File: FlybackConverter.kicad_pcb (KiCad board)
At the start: 2 copper layers, 76.2 x 76.2 mm, 46 parts, among them J1 USB_C_Receptacle_PowerOnly_6P, T1 Transformer_1P_2S, U1 LNK6428K, U2 TPS25820DSST

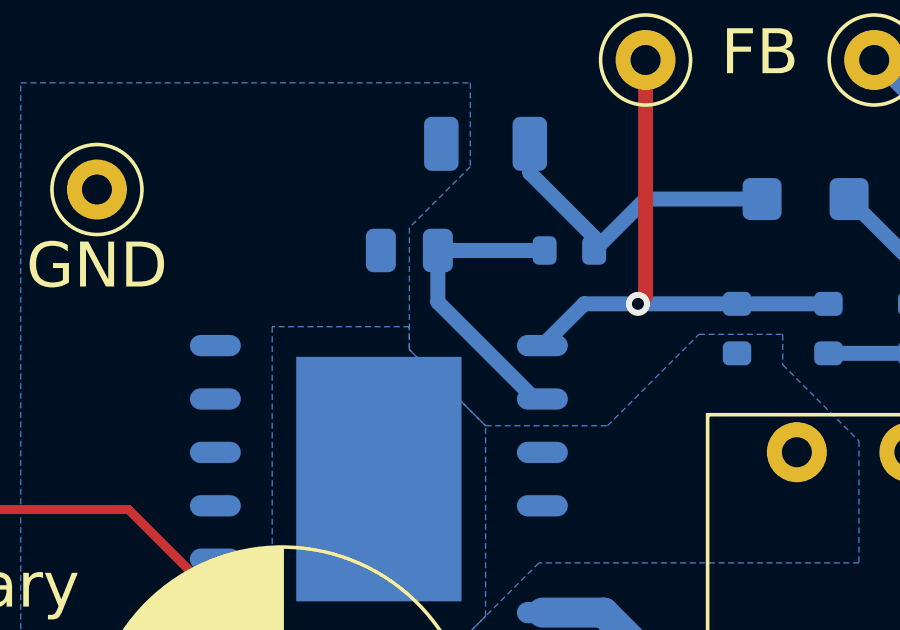
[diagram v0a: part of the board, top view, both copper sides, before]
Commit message: C7のフットプリントを1206に変更 #5
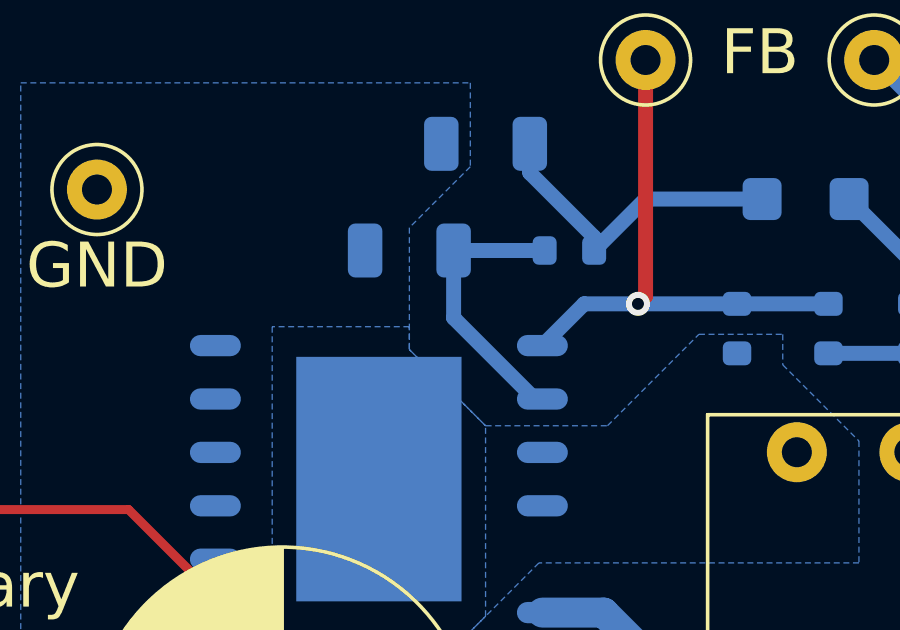
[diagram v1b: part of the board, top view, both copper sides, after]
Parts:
- C7: footprint Capacitor_SMD:C_0805_2012Metric -> Capacitor_SMD:C_1206_3216Metric
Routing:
- net Net-(U1-BP): track 10.1 -> 9.36 mm
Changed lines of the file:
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@@
     )
   )
-  (footprint "Capacitor_SMD:C_0805_2012Metric" (layer "B.Cu")
+  (footprint "Capacitor_SMD:C_1206_3216Metric" (layer "B.Cu")
     (at 147.066 62.23 180)
-    (descr "Capacitor SMD 0805 (2012 Metric), square (rectangular) end terminal, IPC_7351 nominal, (Body size source: IPC-SM-782 page 76, https://www.pcb-3d.com/wordpress/wp-content/uploads/ipc-sm-782a_amendment_1_and_2.pdf, https://docs.google.com/spreadsheets/d/1BsfQQcO9C6DZCsRaXUlFlo91Tg2WpOkGARC1WS5S8t0/edit?usp=sharing), generated with kicad-footprint-generator")
+    (descr "Capacitor SMD 1206 (3216 Metric), square (rectangular) end terminal, IPC_7351 nominal, (Body size source: IPC-SM-782 page 76, https://www.pcb-3d.com/wordpress/wp-content/uploads/ipc-sm-782a_amendment_1_and_2.pdf), generated with kicad-footprint-generator")
     (tags "capacitor")
     (property "Sheetfile" "FlybackConverter.kicad_sch")
@@
     (property "ki_keywords" "cap capacitor")
     (attr smd)
-    (fp_text reference "C7" (at 2.54 0) (layer "B.SilkS")
+    (fp_text reference "C7" (at 0 1.85) (layer "B.SilkS")
         (effects (font (size 1 1) (thickness 0.15)) (justify mirror))
     )
-    (fp_text value "1u" (at -2.985 -3.458) (layer "B.Fab")
+    (fp_text value "1u" (at 0 -1.85) (layer "B.Fab")
         (effects (font (size 1 1) (thickness 0.15)) (justify mirror))
     )
     (fp_text user "${REFERENCE}" (at 0 0) (layer "B.Fab")
-        (effects (font (size 0.5 0.5) (thickness 0.08)) (justify mirror))
+        (effects (font (size 0.8 0.8) (thickness 0.12)) (justify mirror))
     )
-    (fp_line (start -0.261252 -0.735) (end 0.261252 -0.735)
+    (fp_line (start -0.711252 -0.91) (end 0.711252 -0.91)
       (stroke (width 0.12) (type solid)) (layer "B.SilkS"))
-    (fp_line (start -0.261252 0.735) (end 0.261252 0.735)
+    (fp_line (start -0.711252 0.91) (end 0.711252 0.91)
       (stroke (width 0.12) (type solid)) (layer "B.SilkS"))
-    (fp_line (start -1.7 -0.98) (end -1.7 0.98)
+    (fp_line (start -2.3 -1.15) (end -2.3 1.15)
       (stroke (width 0.05) (type solid)) (layer "B.CrtYd"))
-    (fp_line (start -1.7 0.98) (end 1.7 0.98)
+    (fp_line (start -2.3 1.15) (end 2.3 1.15)
       (stroke (width 0.05) (type solid)) (layer "B.CrtYd"))
-    (fp_line (start 1.7 -0.98) (end -1.7 -0.98)
+    (fp_line (start 2.3 -1.15) (end -2.3 -1.15)
       (stroke (width 0.05) (type solid)) (layer "B.CrtYd"))
-    (fp_line (start 1.7 0.98) (end 1.7 -0.98)
+    (fp_line (start 2.3 1.15) (end 2.3 -1.15)
       (stroke (width 0.05) (type solid)) (layer "B.CrtYd"))
-    (fp_line (start -1 -0.625) (end -1 0.625)
+    (fp_line (start -1.6 -0.8) (end -1.6 0.8)
       (stroke (width 0.1) (type solid)) (layer "B.Fab"))
-    (fp_line (start -1 0.625) (end 1 0.625)
+    (fp_line (start -1.6 0.8) (end 1.6 0.8)
       (stroke (width 0.1) (type solid)) (layer "B.Fab"))
-    (fp_line (start 1 -0.625) (end -1 -0.625)
+    (fp_line (start 1.6 -0.8) (end -1.6 -0.8)
       (stroke (width 0.1) (type solid)) (layer "B.Fab"))
-    (fp_line (start 1 0.625) (end 1 -0.625)
+    (fp_line (start 1.6 0.8) (end 1.6 -0.8)
       (stroke (width 0.1) (type solid)) (layer "B.Fab"))
-    (pad "1" smd roundrect (at -0.95 0 180) (size 1 1.45) (layers "B.Cu" "B.Paste" "B.Mask") (roundrect_rratio 0.25)
+    (pad "1" smd roundrect (at -1.475 0 180) (size 1.15 1.8) (layers "B.Cu" "B.Paste" "B.Mask") (roundrect_rratio 0.217391)
       (net 9 "Net-(U1-BP)") (pintype "passive"))
-    (pad "2" smd roundrect (at 0.95 0 180) (size 1 1.45) (layers "B.Cu" "B.Paste" "B.Mask") (roundrect_rratio 0.25)
+    (pad "2" smd roundrect (at 1.475 0 180) (size 1.15 1.8) (layers "B.Cu" "B.Paste" "B.Mask") (roundrect_rratio 0.217391)
       (net 17 "Net-(T1-SB)") (pintype "passive"))
-    (model "${KICAD6_3DMODEL_DIR}/Capacitor_SMD.3dshapes/C_0805_2012Metric.wrl"
+    (model "${KICAD6_3DMODEL_DIR}/Capacitor_SMD.3dshapes/C_1206_3216Metric.wrl"
       (offset (xyz 0 0 0))
       (scale (xyz 1 1 1))
@@
   (segment (start 166.558 93.9755) (end 167.3245 94.742) (width 1) (layer "B.Cu") (net 8))
   (segment (start 166.558 91.186) (end 166.558 93.9755) (width 1) (layer "B.Cu") (net 8))
-  (segment (start 148.016 62.23) (end 151.575 62.23) (width 0.5) (layer "B.Cu") (net 9))
-  (segment (start 148.016 63.95) (end 151.246 67.18) (width 0.5) (layer "B.Cu") (net 9))
+  (segment (start 151.575 62.23) (end 148.541 62.23) (width 0.5) (layer "B.Cu") (net 9))
+  (segment (start 148.541 62.23) (end 148.541 64.475) (width 0.5) (layer "B.Cu") (net 9))
   (segment (start 151.246 67.18) (end 151.5 67.18) (width 0.5) (layer "B.Cu") (net 9))
-  (segment (start 148.016 62.23) (end 148.016 63.95) (width 0.5) (layer "B.Cu") (net 9))
+  (segment (start 148.541 64.475) (end 151.246 67.18) (width 0.5) (layer "B.Cu") (net 9))
   (segment (start 154.94 60.515) (end 158.824 60.515) (width 0.5) (layer "B.Cu") (net 10))
   (segment (start 153.225 62.23) (end 154.94 60.515) (width 0.5) (layer "B.Cu") (net 10))

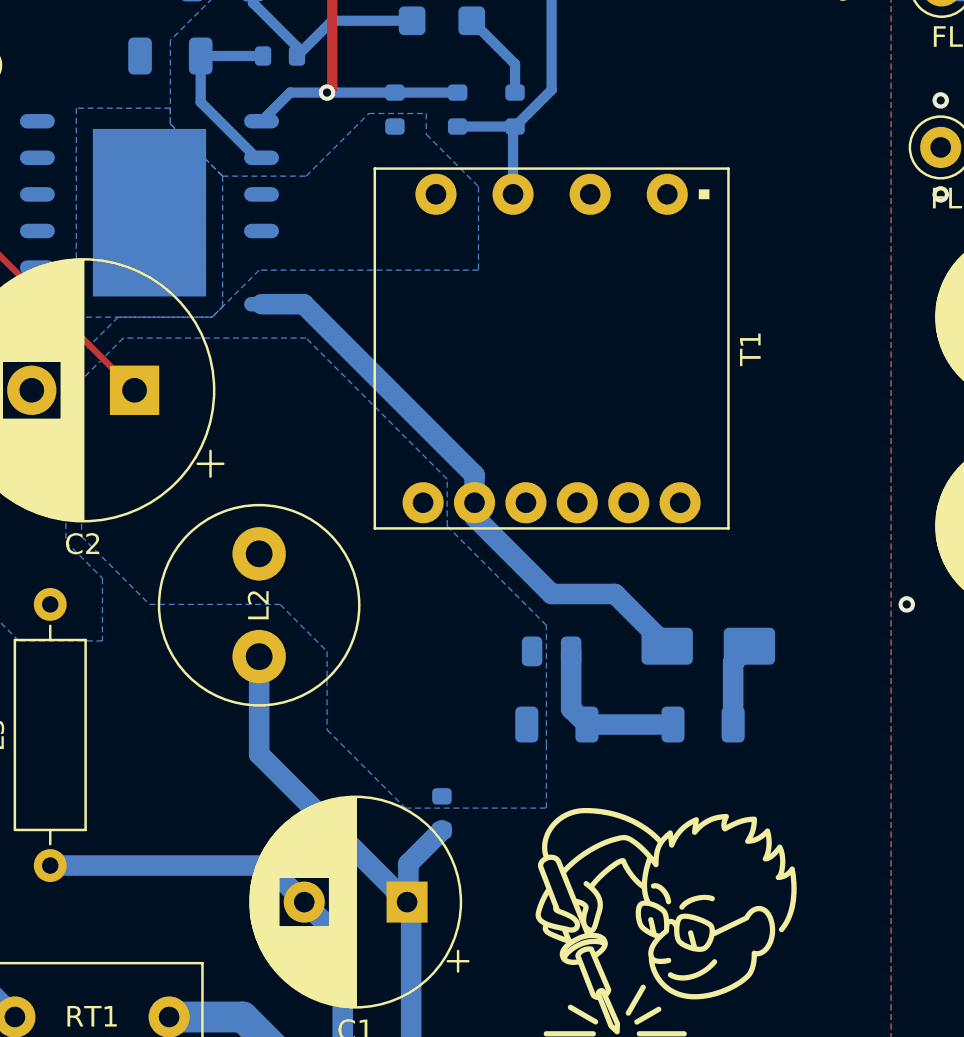
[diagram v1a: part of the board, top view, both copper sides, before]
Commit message: トランスのフットプリント修正、それに合わせて部品配置も調整 fix #6
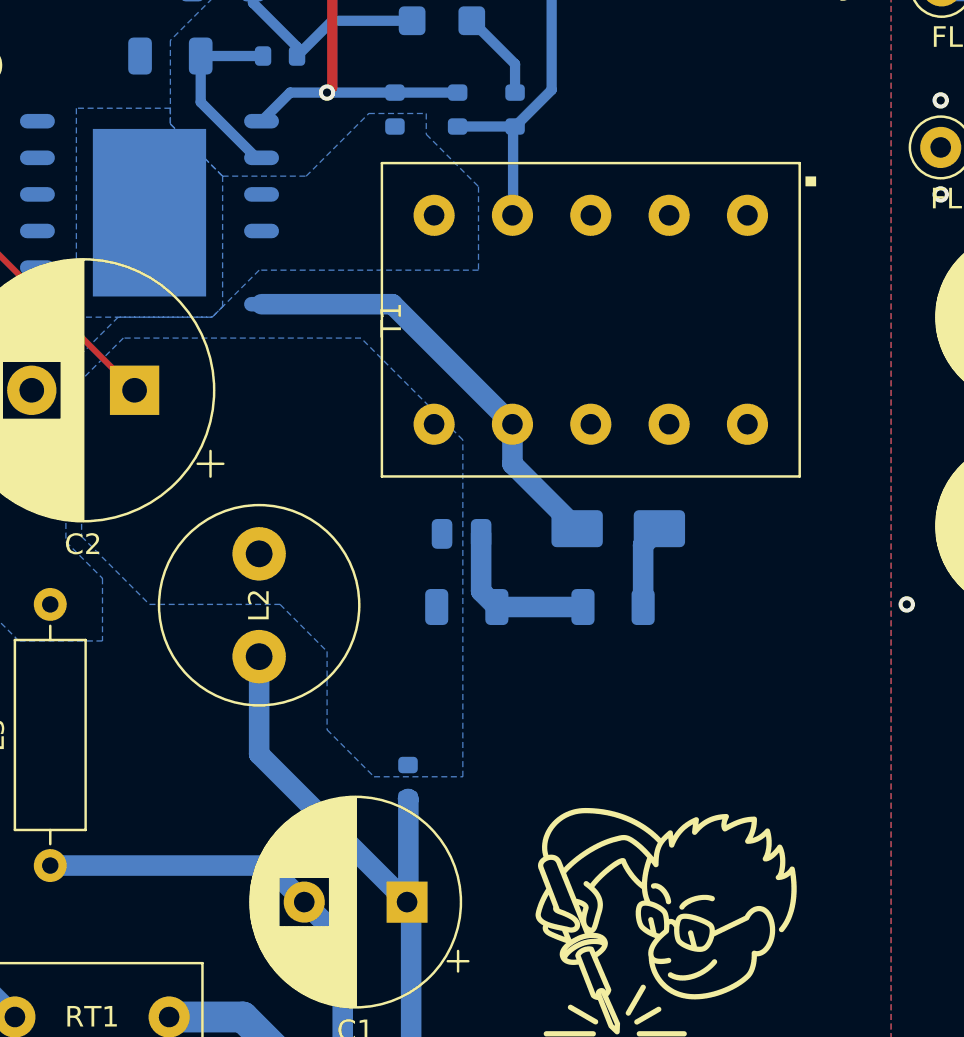
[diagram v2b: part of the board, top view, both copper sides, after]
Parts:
- T1: footprint 00_Library:BEPC17-1110CPHFR -> 00_Library:B66206W1110T001
- moved C6 7.20 mm to (161.2, 85.5)
- moved D2 7.20 mm to (168.8, 85.2)
- moved R11 7.20 mm to (161.5, 89.0)
- moved R3 7.20 mm to (168.6, 89.0)
- moved T1 2.36 mm to (167.5, 75.1), turned to -90 degrees
- moved R10 2.25 mm to (158.6, 97.5)
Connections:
- T1 pad 3: Net-(T1-SA) -> (no net)
- T1 pad 4: Net-(T1-SB) -> Net-(T1-SA)
- T1 pad 5: Net-(T1-AA) -> Net-(T1-SB)
- T1 pad 6: Net-(D2-A) -> Net-(T1-AA)
- T1 pad 7: (no net) -> Net-(D2-A)
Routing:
- net Net-(D2-A): track 27.8 -> 21.0 mm
- net Net-(T1-SA): track 17.9 -> 18.9 mm
- net Net-(BR1-+): track 26.9 -> 27.8 mm
